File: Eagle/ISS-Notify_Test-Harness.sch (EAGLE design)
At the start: 36 parts, among them J1 6HEADER, U1 ATMEGA32U4, U3 TPS63001, X1 8 MHz

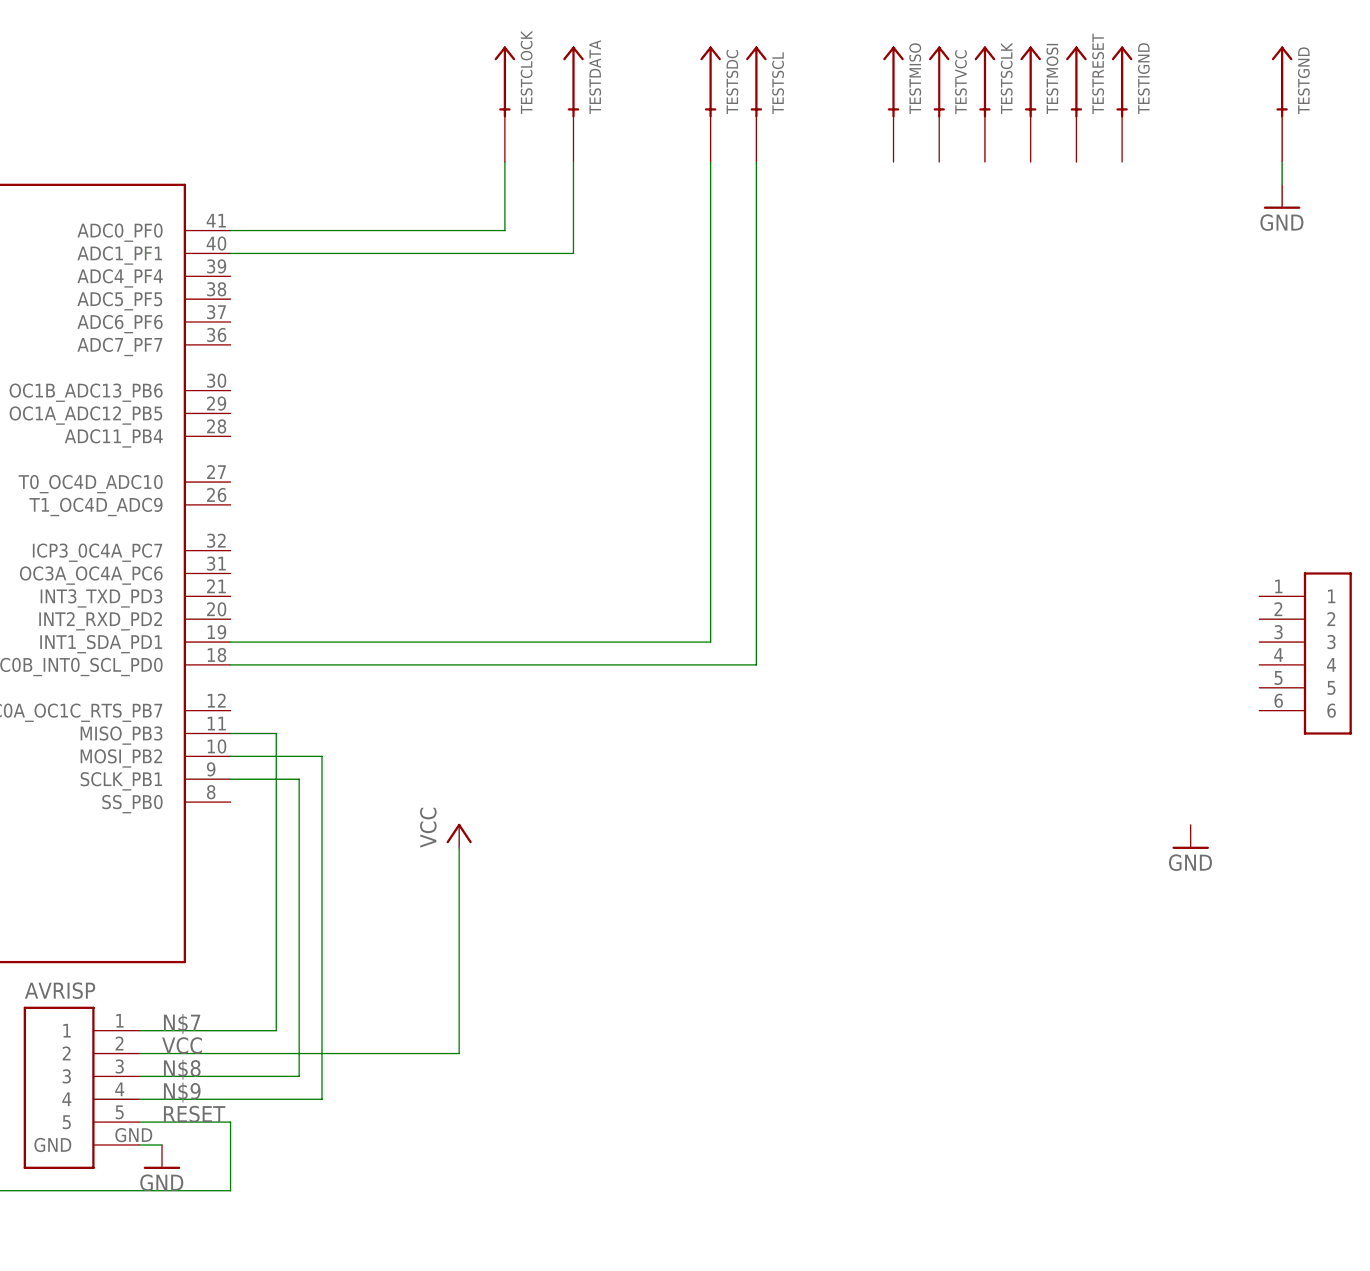
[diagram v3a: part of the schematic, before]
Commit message: external programmer for test board
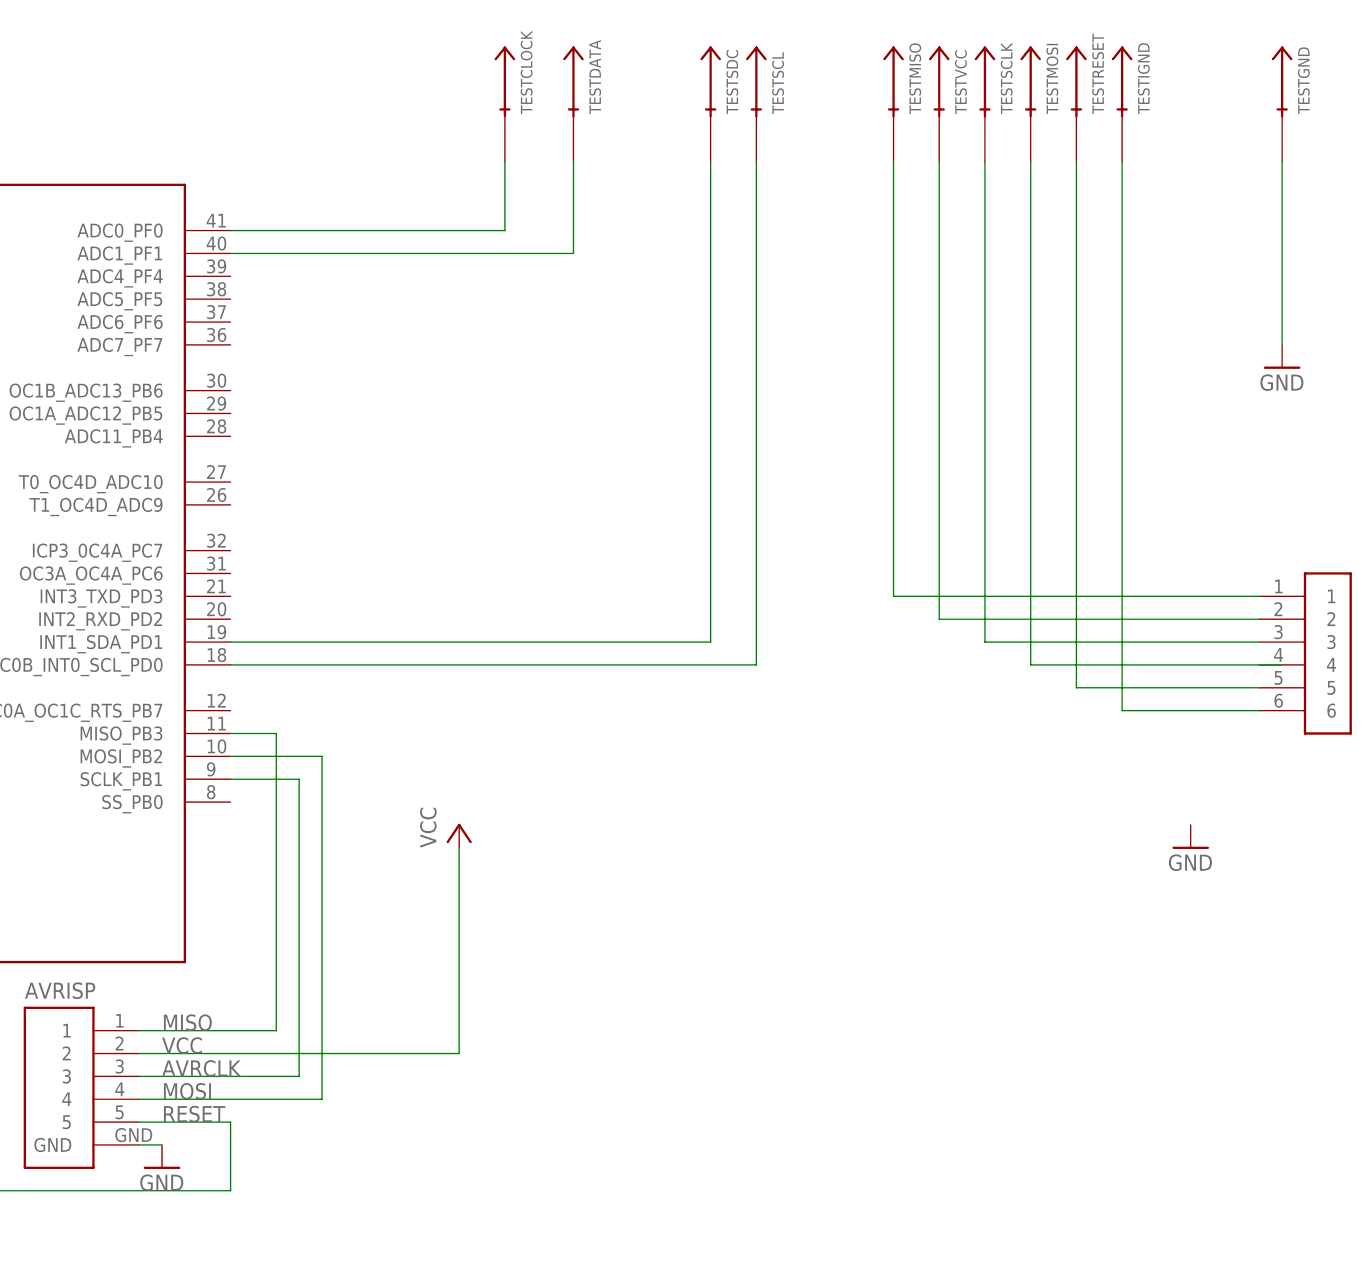
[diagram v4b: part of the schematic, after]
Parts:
- renumbered J1 to JPROGRAMER
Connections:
- net N$7 renamed MISO
- net N$8 renamed AVRCLK
- net N$9 renamed MOSI
- new net TESTGND: JPROGRAMER.6, TESTIGND.TEST
- new net TESTMISO: JPROGRAMER.1, TESTMISO.TEST
- new net TESTMOSI: TESTMOSI.TEST
- new net TESTRESET: JPROGRAMER.5, TESTRESET.TEST
- new net TESTSCLK: JPROGRAMER.3, TESTSCLK.TEST
- new net TESTVCC: JPROGRAMER.2, TESTVCC.TEST
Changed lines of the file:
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@@
 <part name="TESTIGND" library="ISS-Notify" deviceset="POGOPIN" device=""/>
 <part name="GND3" library="supply1" deviceset="GND" device=""/>
-<part name="J1" library="ISS-Notify" deviceset="6HEADER" device=""/>
+<part name="JPROGRAMER" library="ISS-Notify" deviceset="6HEADER" device=""/>
 </parts>
 <sheets>
@@
 <instance part="TESTCLOCK" gate="G$1" x="259.08" y="198.12"/>
 <instance part="TESTGND" gate="G$1" x="345.44" y="198.12"/>
-<instance part="GND23" gate="1" x="345.44" y="193.04"/>
+<instance part="GND23" gate="1" x="345.44" y="175.26"/>
 <instance part="TESTMISO" gate="G$1" x="302.26" y="198.12"/>
 <instance part="TESTVCC" gate="G$1" x="307.34" y="198.12"/>
@@
 <instance part="TESTIGND" gate="G$1" x="327.66" y="198.12"/>
 <instance part="GND3" gate="1" x="335.28" y="121.92"/>
-<instance part="J1" gate="G$1" x="350.52" y="144.78"/>
+<instance part="JPROGRAMER" gate="G$1" x="350.52" y="144.78"/>
 </instances>
 <busses>
@@
 <pinref part="GND23" gate="1" pin="GND"/>
 <pinref part="TESTGND" gate="G$1" pin="TEST"/>
-<wire x1="345.44" y1="195.58" x2="345.44" y2="198.12" width="0.1524" layer="91"/>
+<wire x1="345.44" y1="177.8" x2="345.44" y2="198.12" width="0.1524" layer="91"/>
 </segment>
 </net>
@@
 </segment>
 </net>
-<net name="N$7" class="0">
+<net name="MISO" class="0">
 <segment>
 <pinref part="U1" gate="ATMEGA" pin="MISO_PB3"/>
@@
 </segment>
 </net>
-<net name="N$8" class="0">
+<net name="AVRCLK" class="0">
 <segment>
 <pinref part="AVRISP" gate="G$1" pin="3"/>
@@
 </segment>
 </net>
-<net name="N$9" class="0">
+<net name="MOSI" class="0">
 <segment>
 <pinref part="U1" gate="ATMEGA" pin="MOSI_PB2"/>
@@
 </segment>
 </net>
+<net name="TESTMISO" class="0">
+<segment>
+<pinref part="JPROGRAMER" gate="G$1" pin="1"/>
+<pinref part="TESTMISO" gate="G$1" pin="TEST"/>
+<wire x1="342.9" y1="149.86" x2="302.26" y2="149.86" width="0.1524" layer="91"/>
+<wire x1="302.26" y1="149.86" x2="302.26" y2="198.12" width="0.1524" layer="91"/>
+</segment>
+</net>
+<net name="TESTVCC" class="0">
+<segment>
+<pinref part="JPROGRAMER" gate="G$1" pin="2"/>
+<pinref part="TESTVCC" gate="G$1" pin="TEST"/>
+<wire x1="342.9" y1="147.32" x2="307.34" y2="147.32" width="0.1524" layer="91"/>
+<wire x1="307.34" y1="147.32" x2="307.34" y2="198.12" width="0.1524" layer="91"/>
+</segment>
+</net>
+<net name="TESTSCLK" class="0">
+<segment>
+<pinref part="JPROGRAMER" gate="G$1" pin="3"/>
+<pinref part="TESTSCLK" gate="G$1" pin="TEST"/>
+<wire x1="342.9" y1="144.78" x2="312.42" y2="144.78" width="0.1524" layer="91"/>
+<wire x1="312.42" y1="144.78" x2="312.42" y2="198.12" width="0.1524" layer="91"/>
+</segment>
+</net>
+<net name="TESTMOSI" class="0">
+<segment>
+<pinref part="TESTMOSI" gate="G$1" pin="TEST"/>
+<wire x1="345.44" y1="142.24" x2="317.5" y2="142.24" width="0.1524" layer="91"/>
+<wire x1="317.5" y1="142.24" x2="317.5" y2="198.12" width="0.1524" layer="91"/>
+</segment>
+</net>
+<net name="TESTRESET" class="0">
+<segment>
+<pinref part="JPROGRAMER" gate="G$1" pin="5"/>
+<pinref part="TESTRESET" gate="G$1" pin="TEST"/>
+<wire x1="342.9" y1="139.7" x2="322.58" y2="139.7" width="0.1524" layer="91"/>
+<wire x1="322.58" y1="139.7" x2="322.58" y2="198.12" width="0.1524" layer="91"/>
+</segment>
+</net>
+<net name="TESTGND" class="0">
+<segment>
+<pinref part="JPROGRAMER" gate="G$1" pin="6"/>
+<pinref part="TESTIGND" gate="G$1" pin="TEST"/>
+<wire x1="342.9" y1="137.16" x2="327.66" y2="137.16" width="0.1524" layer="91"/>
+<wire x1="327.66" y1="137.16" x2="327.66" y2="198.12" width="0.1524" layer="91"/>
+</segment>
+</net>
